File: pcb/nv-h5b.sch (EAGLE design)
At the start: 17 parts, among them IC1 TINY13A-20SSU, J1 22-05-7038-03

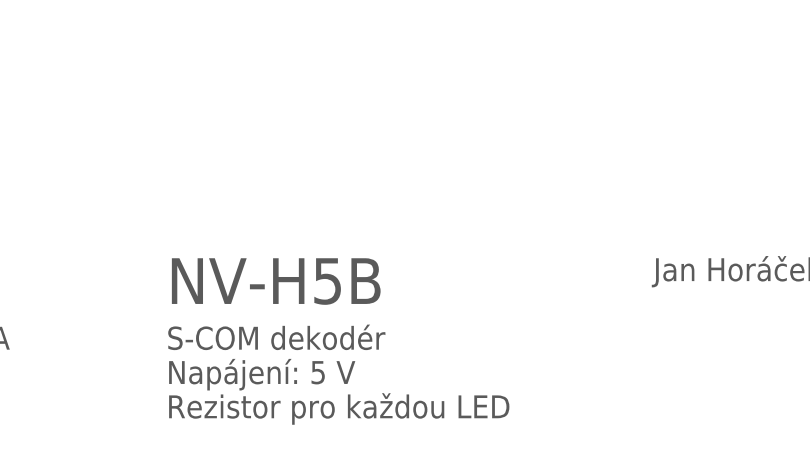
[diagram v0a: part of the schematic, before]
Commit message: PCB: add version.
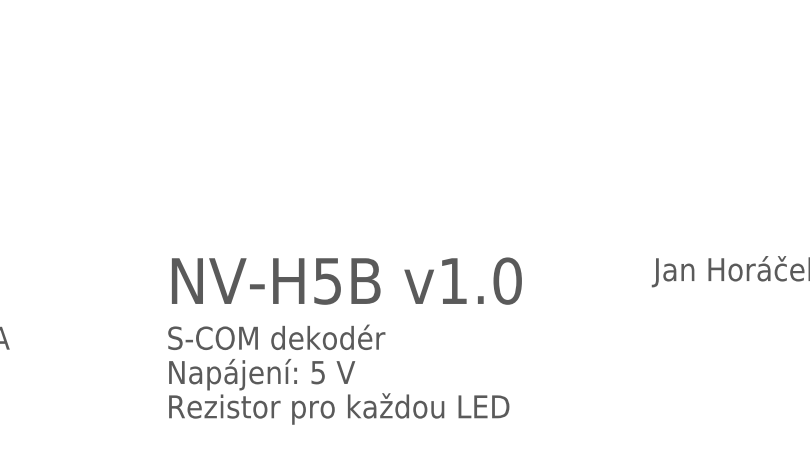
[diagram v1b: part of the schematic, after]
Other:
- note added: "NV-H5B v1.0"
- note removed: "NV-H5B"
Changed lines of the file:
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@@
 <plain>
 <text x="140.462" y="20.32" size="2.54" layer="97">Jan Horáček</text>
-<text x="86.36" y="17.78" size="5.08" layer="97">NV-H5B</text>
+<text x="86.36" y="17.78" size="5.08" layer="97">NV-H5B v1.0</text>
 <text x="86.36" y="5.08" size="2.54" layer="97">S-COM dekodér
 Napájení: 5 V

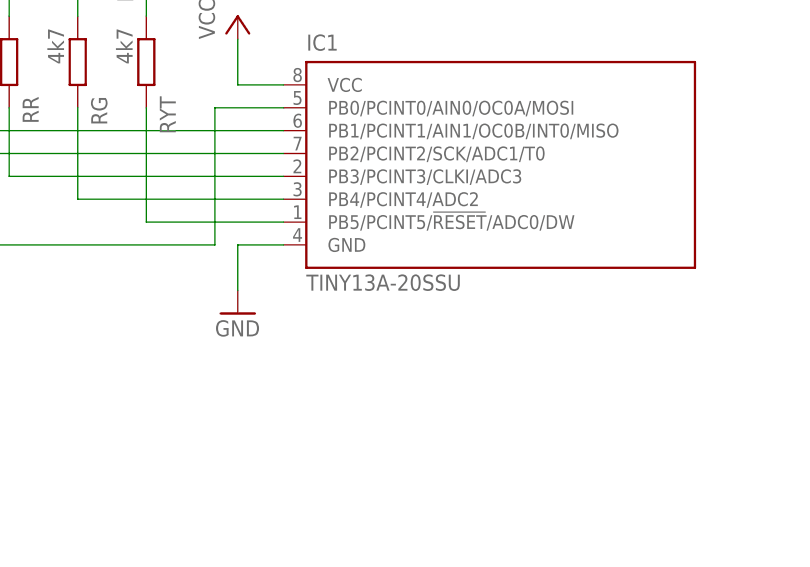
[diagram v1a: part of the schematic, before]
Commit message: sch: use ATtiny25.
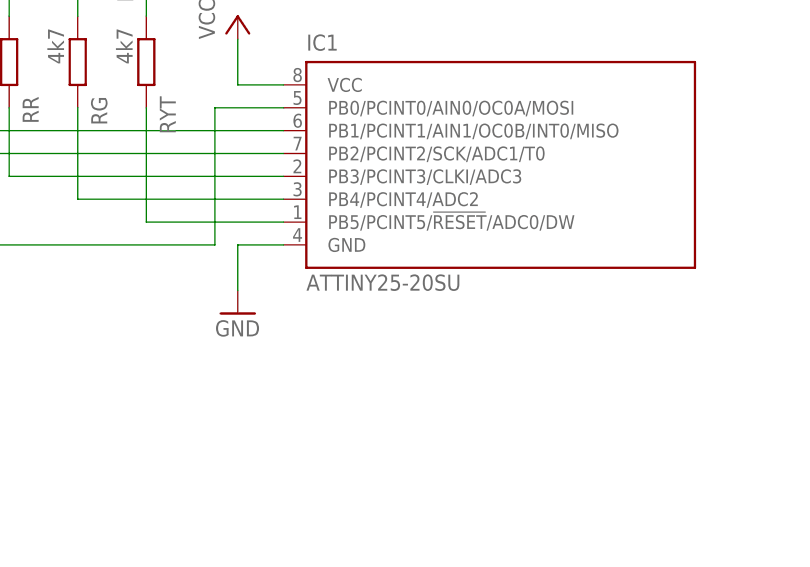
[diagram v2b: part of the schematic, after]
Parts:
- IC1: value TINY13A-20SSU -> ATTINY25-20SU
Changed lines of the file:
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@@
 </classes>
 <parts>
-<part name="IC1" library="atmel" library_urn="urn:adsk.eagle:library:105" deviceset="TINY13" device="SSU" package3d_urn="urn:adsk.eagle:package:4358/1" technology="-20" value="TINY13A-20SSU"/>
+<part name="IC1" library="atmel" library_urn="urn:adsk.eagle:library:105" deviceset="TINY13" device="SSU" package3d_urn="urn:adsk.eagle:package:4358/1" technology="-20" value="ATTINY25-20SU"/>
 <part name="P+1" library="supply1" library_urn="urn:adsk.eagle:library:371" deviceset="VCC" device=""/>
 <part name="GND1" library="supply1" library_urn="urn:adsk.eagle:library:371" deviceset="GND" device=""/>

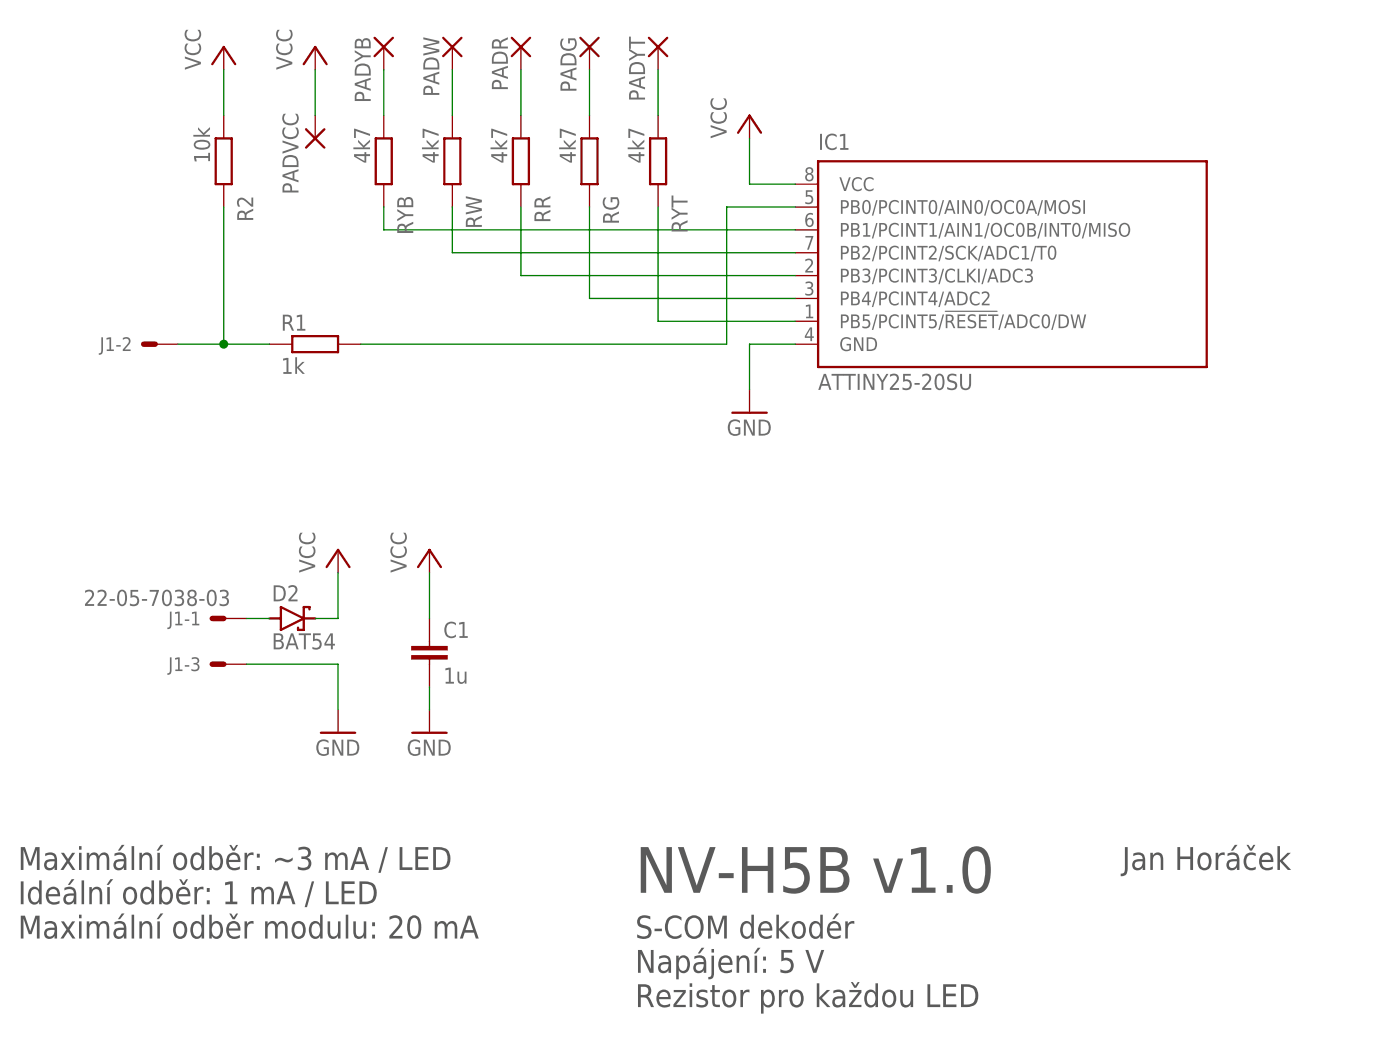
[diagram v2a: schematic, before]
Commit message: Opravit orientaci vstupniho konektoru.
Bylo opacne GND & VCC.
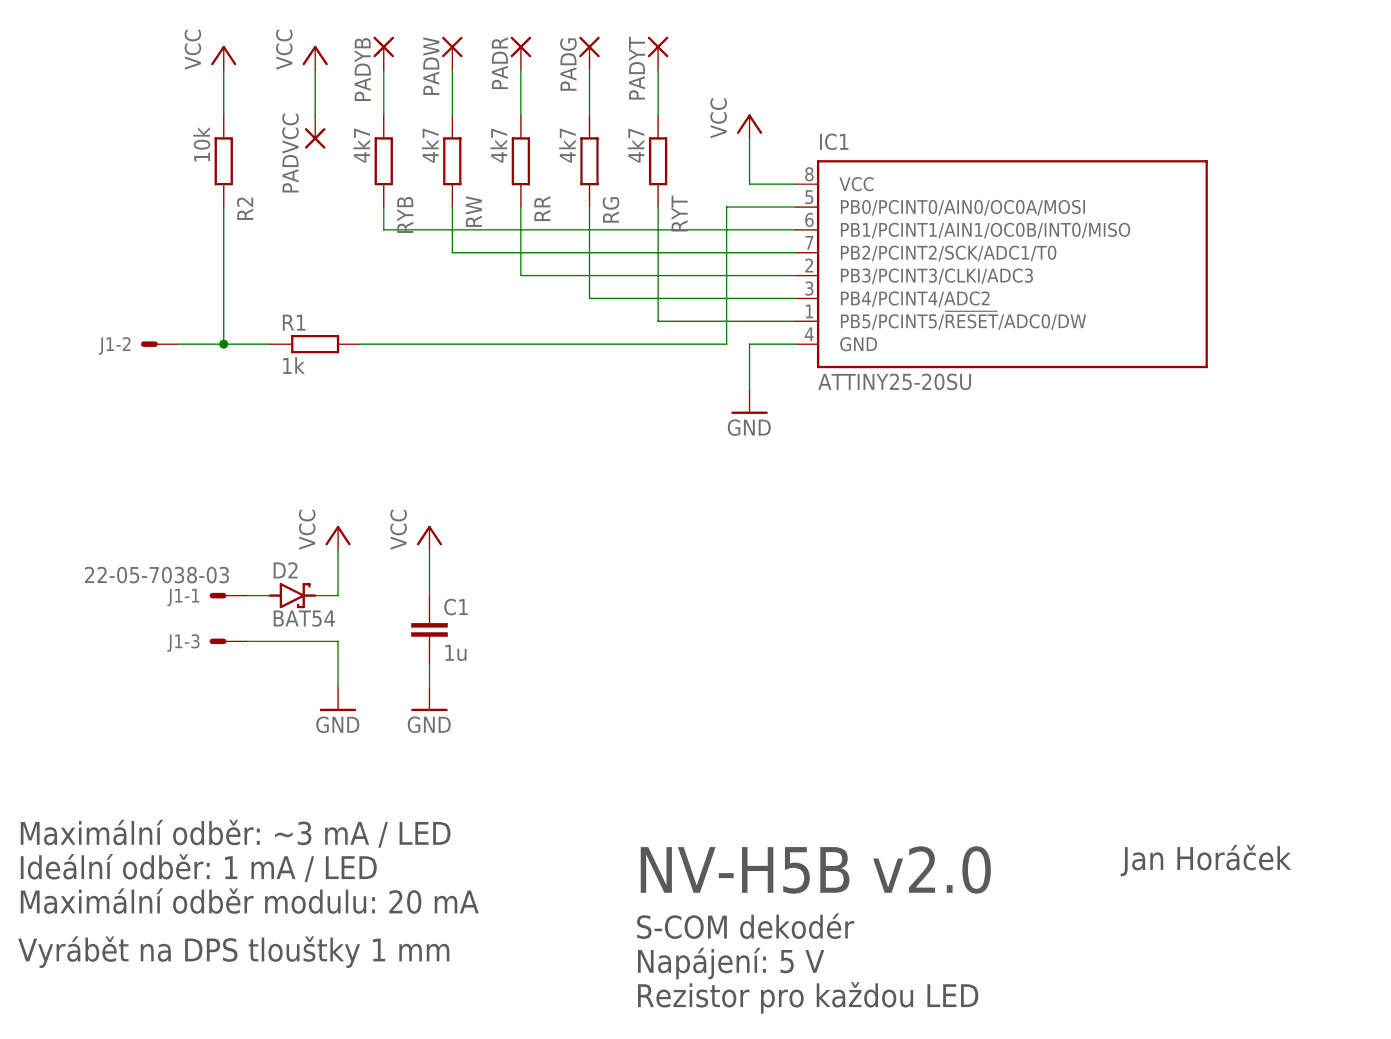
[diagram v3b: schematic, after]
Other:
- note added: "NV-H5B v2.0"
- note added: "Vyrábět na DPS tlouštky 1 mm"
- note removed: "NV-H5B v1.0"
- moved on the sheet: C1, D2, J1-1, J1-3
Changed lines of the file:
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@@
 <plain>
 <text x="140.462" y="20.32" size="2.54" layer="97">Jan Horáček</text>
-<text x="86.36" y="17.78" size="5.08" layer="97">NV-H5B v1.0</text>
+<text x="86.36" y="17.78" size="5.08" layer="97">NV-H5B v2.0</text>
 <text x="86.36" y="5.08" size="2.54" layer="97">S-COM dekodér
 Napájení: 5 V
 Rezistor pro každou LED</text>
-<text x="17.78" y="12.7" size="2.54" layer="97">Maximální odběr: ~3 mA / LED
+<text x="17.78" y="15.494" size="2.54" layer="97">Maximální odběr: ~3 mA / LED
 Ideální odběr: 1 mA / LED
 Maximální odběr modulu: 20 mA</text>
+<text x="17.78" y="10.16" size="2.54" layer="97">Vyrábět na DPS tlouštky 1 mm</text>
 </plain>
 <instances>
@@
 <attribute name="VALUE" x="96.52" y="68.58" size="1.778" layer="96"/>
 </instance>
-<instance part="C1" gate="G$1" x="63.5" y="45.72" smashed="yes">
-<attribute name="NAME" x="65.024" y="46.101" size="1.778" layer="95"/>
-<attribute name="VALUE" x="65.024" y="41.021" size="1.778" layer="96"/>
-</instance>
-<instance part="P+2" gate="VCC" x="63.5" y="55.88" smashed="yes">
-<attribute name="VALUE" x="60.96" y="53.34" size="1.778" layer="96" rot="R90"/>
-</instance>
-<instance part="GND2" gate="1" x="63.5" y="35.56" smashed="yes">
-<attribute name="VALUE" x="60.96" y="33.02" size="1.778" layer="96"/>
+<instance part="C1" gate="G$1" x="63.5" y="48.26" smashed="yes">
+<attribute name="NAME" x="65.024" y="48.641" size="1.778" layer="95"/>
+<attribute name="VALUE" x="65.024" y="43.561" size="1.778" layer="96"/>
+</instance>
+<instance part="P+2" gate="VCC" x="63.5" y="58.42" smashed="yes">
+<attribute name="VALUE" x="60.96" y="55.88" size="1.778" layer="96" rot="R90"/>
+</instance>
+<instance part="GND2" gate="1" x="63.5" y="38.1" smashed="yes">
+<attribute name="VALUE" x="60.96" y="35.56" size="1.778" layer="96"/>
 </instance>
 <instance part="RR" gate="G$1" x="73.66" y="99.06" smashed="yes" rot="R270">
@@
 <attribute name="VALUE" x="38.1" y="109.22" size="1.778" layer="96" rot="R90"/>
 </instance>
-<instance part="J1" gate="-1" x="40.64" y="48.26" smashed="yes" rot="MR0">
-<attribute name="NAME" x="38.1" y="47.498" size="1.524" layer="95" rot="MR0"/>
-<attribute name="VALUE" x="41.402" y="49.657" size="1.778" layer="96" rot="MR0"/>
+<instance part="J1" gate="-1" x="40.64" y="50.8" smashed="yes" rot="MR0">
+<attribute name="NAME" x="38.1" y="50.038" size="1.524" layer="95" rot="MR0"/>
+<attribute name="VALUE" x="41.402" y="52.197" size="1.778" layer="96" rot="MR0"/>
 </instance>
 <instance part="J1" gate="-2" x="33.02" y="78.74" smashed="yes" rot="MR0">
 <attribute name="NAME" x="30.48" y="77.978" size="1.524" layer="95" rot="MR0"/>
 </instance>
-<instance part="J1" gate="-3" x="40.64" y="43.18" smashed="yes" rot="MR0">
-<attribute name="NAME" x="38.1" y="42.418" size="1.524" layer="95" rot="MR0"/>
-</instance>
-<instance part="P+4" gate="VCC" x="53.34" y="55.88" smashed="yes">
-<attribute name="VALUE" x="50.8" y="53.34" size="1.778" layer="96" rot="R90"/>
-</instance>
-<instance part="GND3" gate="1" x="53.34" y="35.56" smashed="yes">
-<attribute name="VALUE" x="50.8" y="33.02" size="1.778" layer="96"/>
+<instance part="J1" gate="-3" x="40.64" y="45.72" smashed="yes" rot="MR0">
+<attribute name="NAME" x="38.1" y="44.958" size="1.524" layer="95" rot="MR0"/>
+</instance>
+<instance part="P+4" gate="VCC" x="53.34" y="58.42" smashed="yes">
+<attribute name="VALUE" x="50.8" y="55.88" size="1.778" layer="96" rot="R90"/>
+</instance>
+<instance part="GND3" gate="1" x="53.34" y="38.1" smashed="yes">
+<attribute name="VALUE" x="50.8" y="35.56" size="1.778" layer="96"/>
 </instance>
 <instance part="FRAME2" gate="G$1" x="0" y="0" smashed="yes">
@@
 <attribute name="VALUE" x="48.26" y="109.22" size="1.778" layer="96" rot="R90"/>
 </instance>
-<instance part="D2" gate="G$1" x="48.26" y="48.26" smashed="yes">
-<attribute name="NAME" x="45.974" y="50.165" size="1.778" layer="95"/>
-<attribute name="VALUE" x="45.974" y="44.831" size="1.778" layer="96"/>
+<instance part="D2" gate="G$1" x="48.26" y="50.8" smashed="yes">
+<attribute name="NAME" x="45.974" y="52.705" size="1.778" layer="95"/>
+<attribute name="VALUE" x="45.974" y="47.371" size="1.778" layer="96"/>
 </instance>
 </instances>
@@
 <pinref part="C1" gate="G$1" pin="1"/>
 <pinref part="P+2" gate="VCC" pin="VCC"/>
-<wire x1="63.5" y1="48.26" x2="63.5" y2="53.34" width="0.1524" layer="91"/>
+<wire x1="63.5" y1="50.8" x2="63.5" y2="55.88" width="0.1524" layer="91"/>
 </segment>
 <segment>
@@
 </segment>
 <segment>
-<wire x1="50.8" y1="48.26" x2="53.34" y2="48.26" width="0.1524" layer="91"/>
+<wire x1="50.8" y1="50.8" x2="53.34" y2="50.8" width="0.1524" layer="91"/>
 <pinref part="P+4" gate="VCC" pin="VCC"/>
-<wire x1="53.34" y1="48.26" x2="53.34" y2="53.34" width="0.1524" layer="91"/>
+<wire x1="53.34" y1="50.8" x2="53.34" y2="55.88" width="0.1524" layer="91"/>
 <pinref part="D2" gate="G$1" pin="C"/>
 </segment>
@@
 <pinref part="GND2" gate="1" pin="GND"/>
 <pinref part="C1" gate="G$1" pin="2"/>
-<wire x1="63.5" y1="38.1" x2="63.5" y2="40.64" width="0.1524" layer="91"/>
+<wire x1="63.5" y1="40.64" x2="63.5" y2="43.18" width="0.1524" layer="91"/>
 </segment>
 <segment>
 <pinref part="J1" gate="-3" pin="S"/>
-<wire x1="43.18" y1="43.18" x2="53.34" y2="43.18" width="0.1524" layer="91"/>
+<wire x1="43.18" y1="45.72" x2="53.34" y2="45.72" width="0.1524" layer="91"/>
 <pinref part="GND3" gate="1" pin="GND"/>
-<wire x1="53.34" y1="43.18" x2="53.34" y2="38.1" width="0.1524" layer="91"/>
+<wire x1="53.34" y1="45.72" x2="53.34" y2="40.64" width="0.1524" layer="91"/>
 </segment>
 </net>
@@
 <segment>
 <pinref part="J1" gate="-1" pin="S"/>
-<wire x1="45.72" y1="48.26" x2="43.18" y2="48.26" width="0.1524" layer="91"/>
+<wire x1="45.72" y1="50.8" x2="43.18" y2="50.8" width="0.1524" layer="91"/>
 <pinref part="D2" gate="G$1" pin="A"/>
 </segment>
